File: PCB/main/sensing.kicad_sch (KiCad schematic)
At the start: 4 parts, among them U4 LM61BIZ/NOPD_TempSensor(TO-92), U5 LPS22HBTR_Barometer

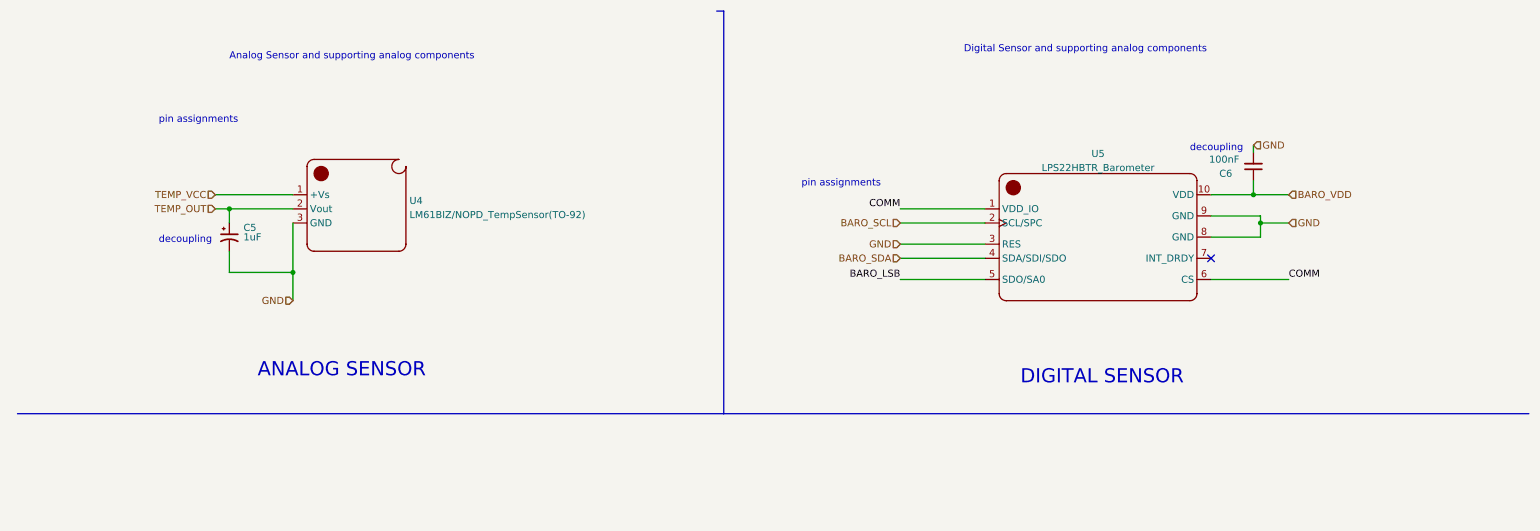
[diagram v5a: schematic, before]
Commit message: Updated all footprints of components
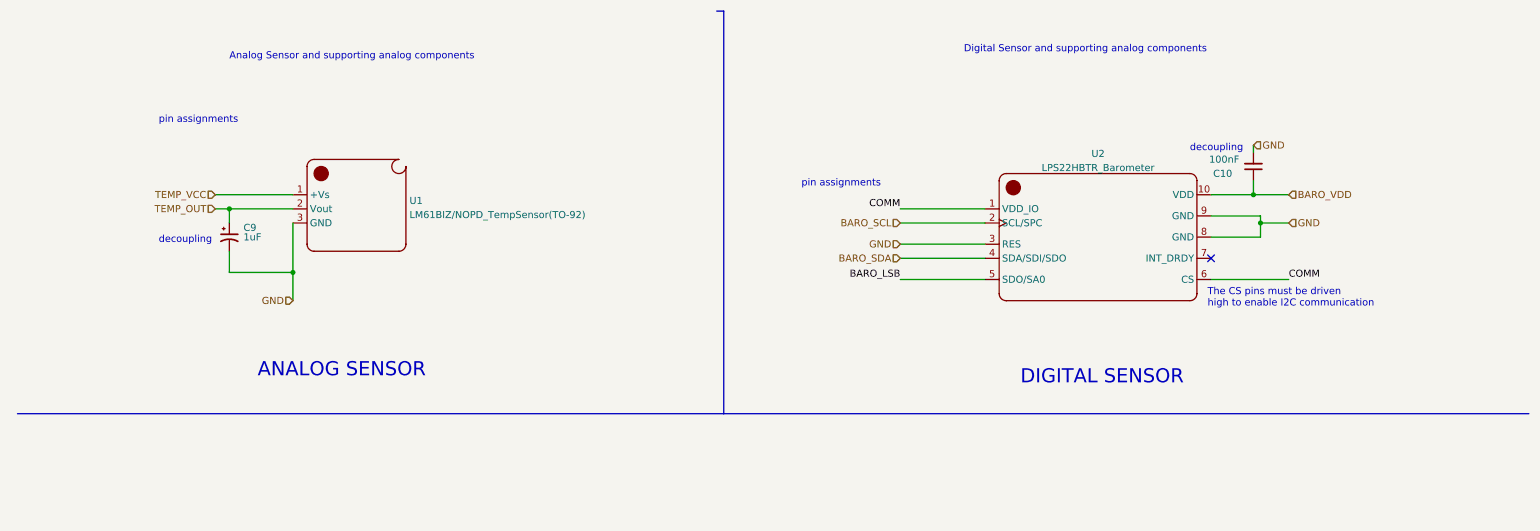
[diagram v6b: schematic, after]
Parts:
- C10: renamed from C6; footprint (none) -> EEE3088F_Footprints:CAPC1005X55N
- C9: renamed from C5; footprint (none) -> EEE3088F_Footprints:RESC1608X55N
- U1: renamed from U4; footprint (none) -> EEE3088F_Footprints:TO-92-3_L4.9-W3.7-P1.27-L
- U2: renamed from U5; footprint (none) -> EEE3088F_Footprints:QFN50P210X200X80-10N
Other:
- note added: "The CS pins must be driven high to enable I2C communication"
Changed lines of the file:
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@@
     (effects (font (size 2.54 2.54)) (justify left bottom))
+  )
+  (text "The CS pins must be driven\nhigh to enable I2C communication"
+    (at 226.695 64.77 0)
+    (effects (font (size 1.27 1.27)) (justify left bottom))
   )
   (text "decoupling" (at 38.1 53.34 0)
@@
   (symbol (lib_id "AAA 3088F:TO-92_Temperature_Sensor") (at 73.66 46.99 0) (unit 1)
     (in_bom yes) (on_board yes) (fields_autoplaced)
-    (property "Reference" "U4" (id 0) (at 83.1851 45.5203 0)
+    (property "Reference" "U1" (id 0) (at 83.1851 45.5203 0)
       (effects (font (size 1.27 1.27)) (justify left))
     )
@@
       (effects (font (size 1.27 1.27)) (justify left))
     )
-    (property "Footprint" "" (id 2) (at 73.66 46.99 0)
+    (property "Footprint" "EEE3088F_Footprints:TO-92-3_L4.9-W3.7-P1.27-L" (id 2) (at 73.66 46.99 0)
       (effects (font (size 1.27 1.27)) hide)
     )
@@
   (symbol (lib_id "AAA 3088F:_C94049_Barometer") (at 207.01 54.61 0) (unit 1)
     (in_bom yes) (on_board yes) (fields_autoplaced)
-    (property "Reference" "U5" (id 0) (at 207.01 37.0671 0))
+    (property "Reference" "U2" (id 0) (at 207.01 37.0671 0))
     (property "Value" "LPS22HBTR_Barometer" (id 1) (at 207.01 39.604 0))
-    (property "Footprint" "" (id 2) (at 207.01 54.61 0)
+    (property "Footprint" "EEE3088F_Footprints:QFN50P210X200X80-10N" (id 2) (at 207.01 54.61 0)
       (effects (font (size 1.27 1.27)) hide)
     )
@@
   (symbol (lib_id "Device:C_Polarized_Small_US") (at 50.8 52.07 0) (unit 1)
     (in_bom yes) (on_board yes)
-    (property "Reference" "C5" (id 0) (at 53.34 50.3681 0)
+    (property "Reference" "C9" (id 0) (at 53.34 50.3681 0)
       (effects (font (size 1.27 1.27)) (justify left))
     )
@@
       (effects (font (size 1.27 1.27)) (justify left))
     )
-    (property "Footprint" "" (id 2) (at 50.8 52.07 0)
+    (property "Footprint" "EEE3088F_Footprints:RESC1608X55N" (id 2) (at 50.8 52.07 0)
       (effects (font (size 1.27 1.27)) hide)
     )
@@
   (symbol (lib_id "Device:C_Small") (at 234.95 39.37 180) (unit 1)
     (in_bom yes) (on_board yes)
-    (property "Reference" "C6" (id 0) (at 231.14 40.64 0)
+    (property "Reference" "C10" (id 0) (at 231.14 40.64 0)
       (effects (font (size 1.27 1.27)) (justify left))
     )
@@
       (effects (font (size 1.27 1.27)) (justify left))
     )
-    (property "Footprint" "" (id 2) (at 234.95 39.37 0)
+    (property "Footprint" "EEE3088F_Footprints:CAPC1005X55N" (id 2) (at 234.95 39.37 0)
       (effects (font (size 1.27 1.27)) hide)
     )

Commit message: Updated labels on schematic
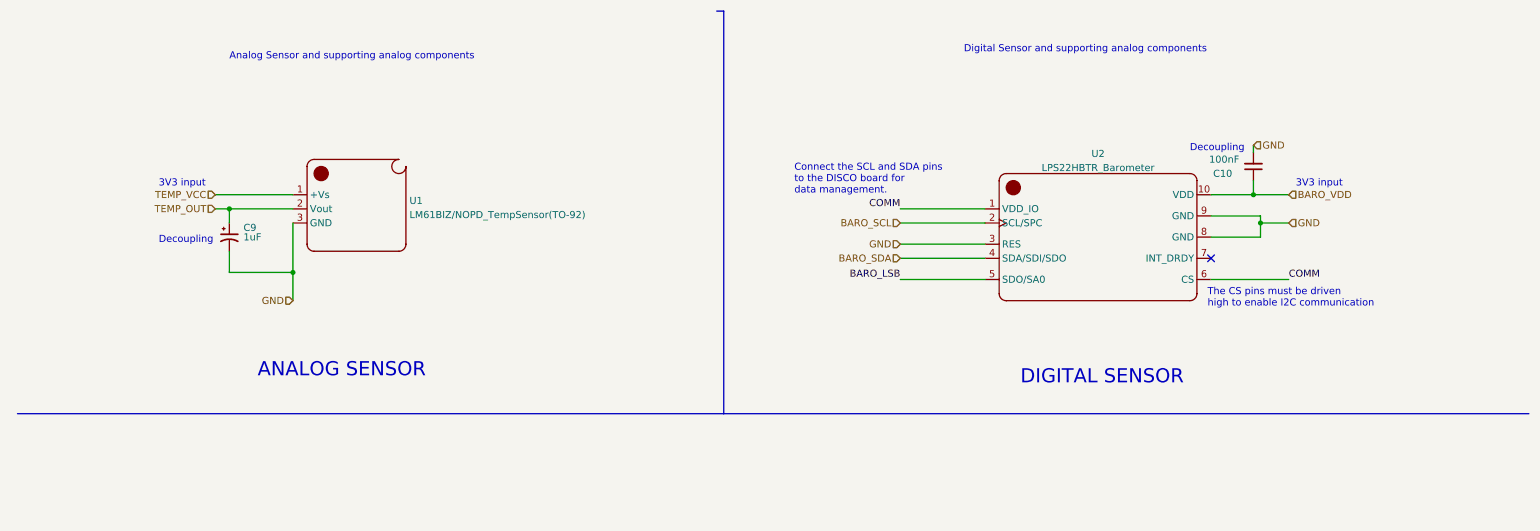
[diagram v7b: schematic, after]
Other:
- note added: "3V3 input"
- note added: "Connect the SCL and SDA pins to the DISCO board for data management."
- note added: "Decoupling"
- note removed: "decoupling"
- note removed: "pin assignments"
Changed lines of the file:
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@@
     (title "Sensing Subsystem")
     (date "2022-03-11")
-    (rev "V0.2")
+    (rev "V0.3")
     (company "University of Cape Town")
     (comment 1 "@Author Caide Spriestersbach (SPRCAI002)")
@@
     (effects (font (size 2.54 2.54)) (justify left bottom))
   )
-  (text "decoupling" (at 223.52 36.83 0)
+  (text "Decoupling\n" (at 223.52 36.83 0)
     (effects (font (size 1.27 1.27)) (justify left bottom))
   )
@@
     (effects (font (size 1.27 1.27)) (justify left bottom))
   )
+  (text "3V3 input\n" (at 242.57 43.18 0)
+    (effects (font (size 1.27 1.27)) (justify left bottom))
+  )
   (text "ANALOG SENSOR" (at 55.88 77.47 0)
     (effects (font (size 2.54 2.54)) (justify left bottom))
+  )
+  (text "3V3 input\n" (at 38.1 43.18 0)
+    (effects (font (size 1.27 1.27)) (justify left bottom))
   )
   (text "The CS pins must be driven\nhigh to enable I2C communication"
@@
     (effects (font (size 1.27 1.27)) (justify left bottom))
   )
-  (text "decoupling" (at 38.1 53.34 0)
+  (text "Decoupling" (at 38.1 53.34 0)
     (effects (font (size 1.27 1.27)) (justify left bottom))
   )
@@
     (effects (font (size 1.27 1.27)) (justify left bottom))
   )
-  (text "pin assignments" (at 153.67 43.18 0)
+  (text "Connect the SCL and SDA pins\nto the DISCO board for\ndata management."
+    (at 152.4 44.45 0)
     (effects (font (size 1.27 1.27)) (justify left bottom))
   )
-  (text "pin assignments" (at 38.1 31.75 0)
-    (effects (font (size 1.27 1.27)) (justify left bottom))
-  )
